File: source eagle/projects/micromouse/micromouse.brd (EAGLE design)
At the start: 100 x 100 mm, 59 parts

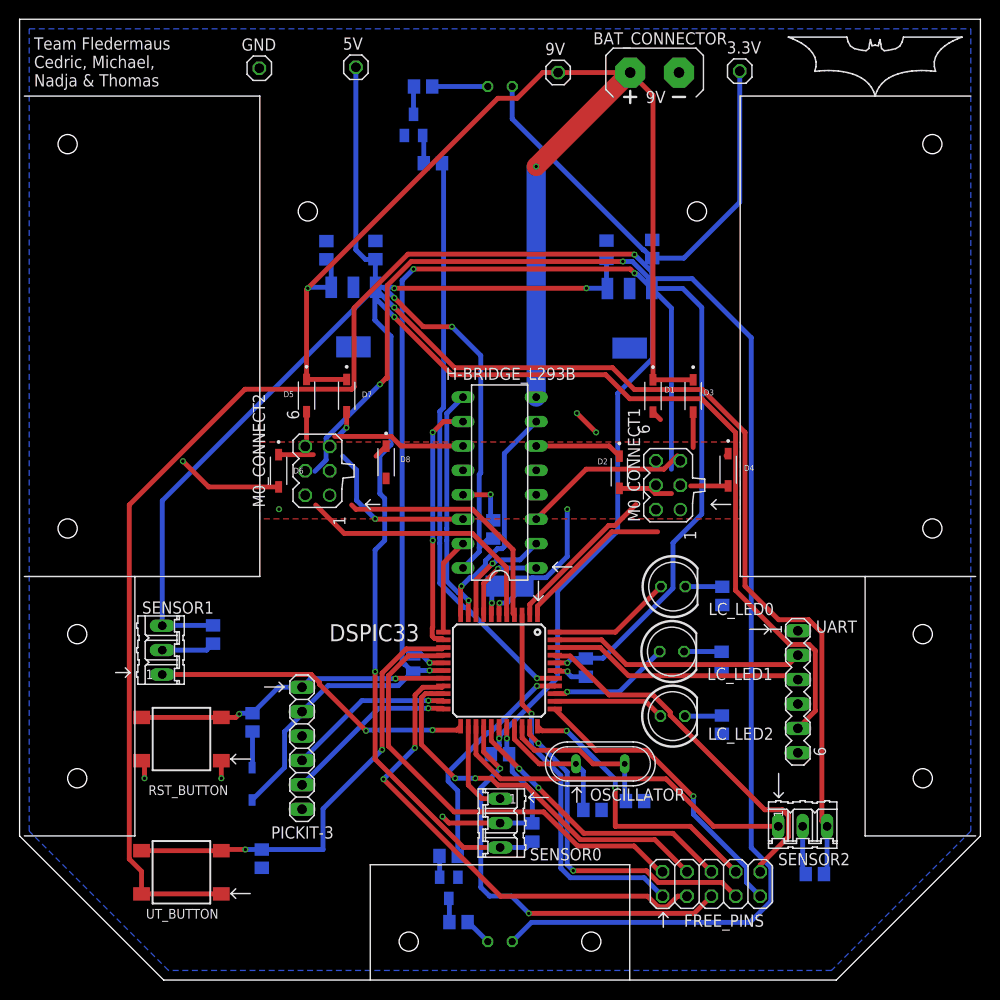
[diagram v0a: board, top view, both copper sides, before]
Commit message: better board design, capacitor missing
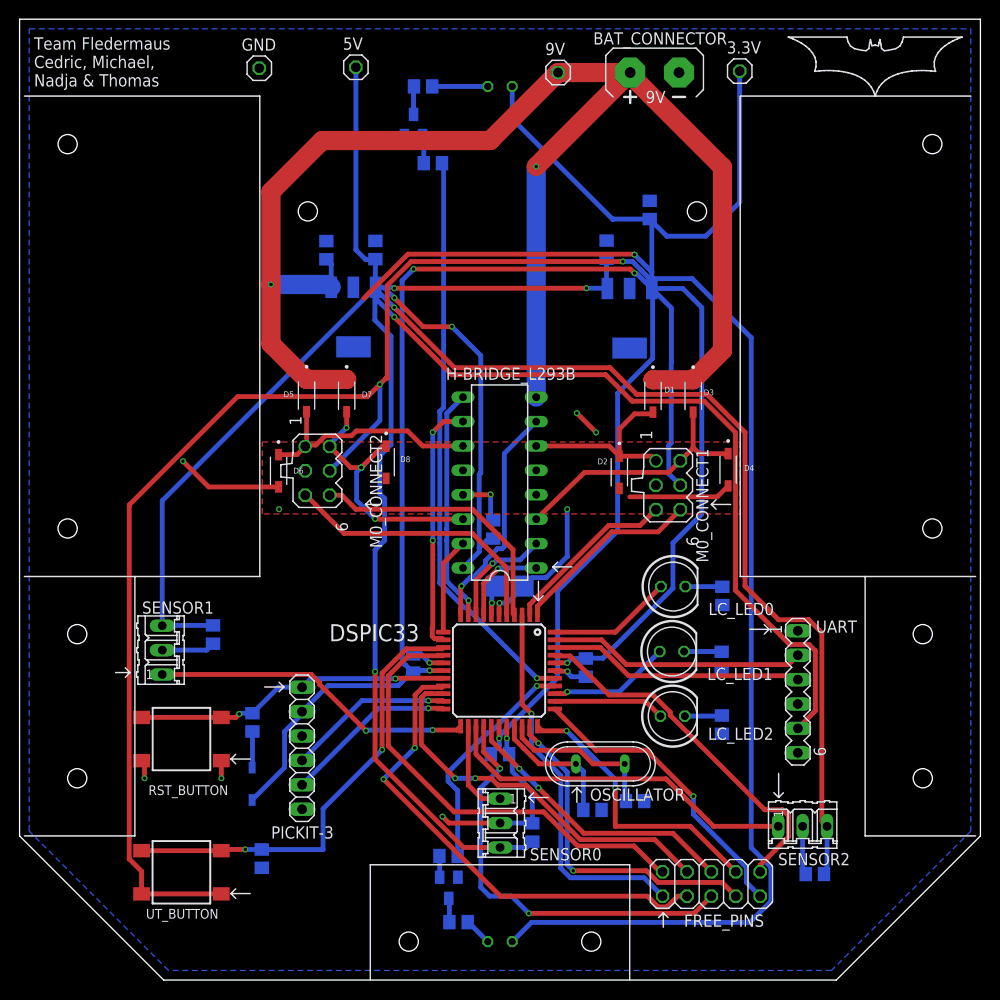
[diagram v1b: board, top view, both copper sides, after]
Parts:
- moved C9 4.07 mm to (65.6, 80.1)
- turned M0_CONNECT1 to 270 degrees
- turned M0_CONNECT2 to 270 degrees
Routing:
- net +9V: track 137.1 -> 156.5 mm
- net M0-: track 10.2 -> 20.2 mm
- net M1+: track 21.3 -> 27.5 mm, vias 2 -> 5
- net M0+: track 21.4 -> 27.3 mm
- net ENC0A: track 16.6 -> 19.9 mm
- net M1-: track 21.2 -> 24.3 mm
- net +3V3: track 551.5 -> 548.6 mm
- net ENC1A: track 25.6 -> 28.3 mm
- net ENC0B: track 16.4 -> 18.6 mm
- net ENC1B: track 27.5 -> 29.0 mm
- net GND: track 84.0 -> 85.2 mm

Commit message: Board fertig, vllt noch silk?
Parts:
- C8: value 0.33µF -> 0.47µF
- C9: value 0.1µF -> 33µF; device rcl:C0805 -> rcl:D/7343-31W
- moved C9 1.55 mm to (66.1, 81.6), turned to 270 degrees
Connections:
- net +3V3: now also C9.+; no longer C9.1
- net GND: now also C9.-; no longer C9.2
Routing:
- net GND: track 85.2 -> 74.6 mm, vias 10 -> 11
- net +3V3: track 548.6 -> 557.4 mm
- net M1+: vias 5 -> 3

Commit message: small changes to board and matlab files
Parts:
- moved M0_CONNECT2 0.80 mm to (31.8, 52.7)
- moved D6 0.25 mm to (26.7, 53.0)
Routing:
- net M1-: track 24.3 -> 27.0 mm
- net M1+: track 27.5 -> 26.6 mm
- net ENC1A: track 28.3 -> 27.4 mm
- net ENC1B: track 29.0 -> 28.4 mm
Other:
- board text added: "MicroMouse 2020"
- board text removed: "Team Fledermaus Cedric, Michael, Nadja & Thomas"
